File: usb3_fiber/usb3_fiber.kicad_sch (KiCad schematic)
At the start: 64 parts, among them J1 U77A16382001, J2 UE76A202000T, J3 10118194-0001LF, J4 GSB4211311WEU, J5 GSB3111311HR, Q1 MMBT3906, U1 MCP2221AT-I/ML, U2 DS100BR111SQE/NOPB, U4 LD1086D2T33TR

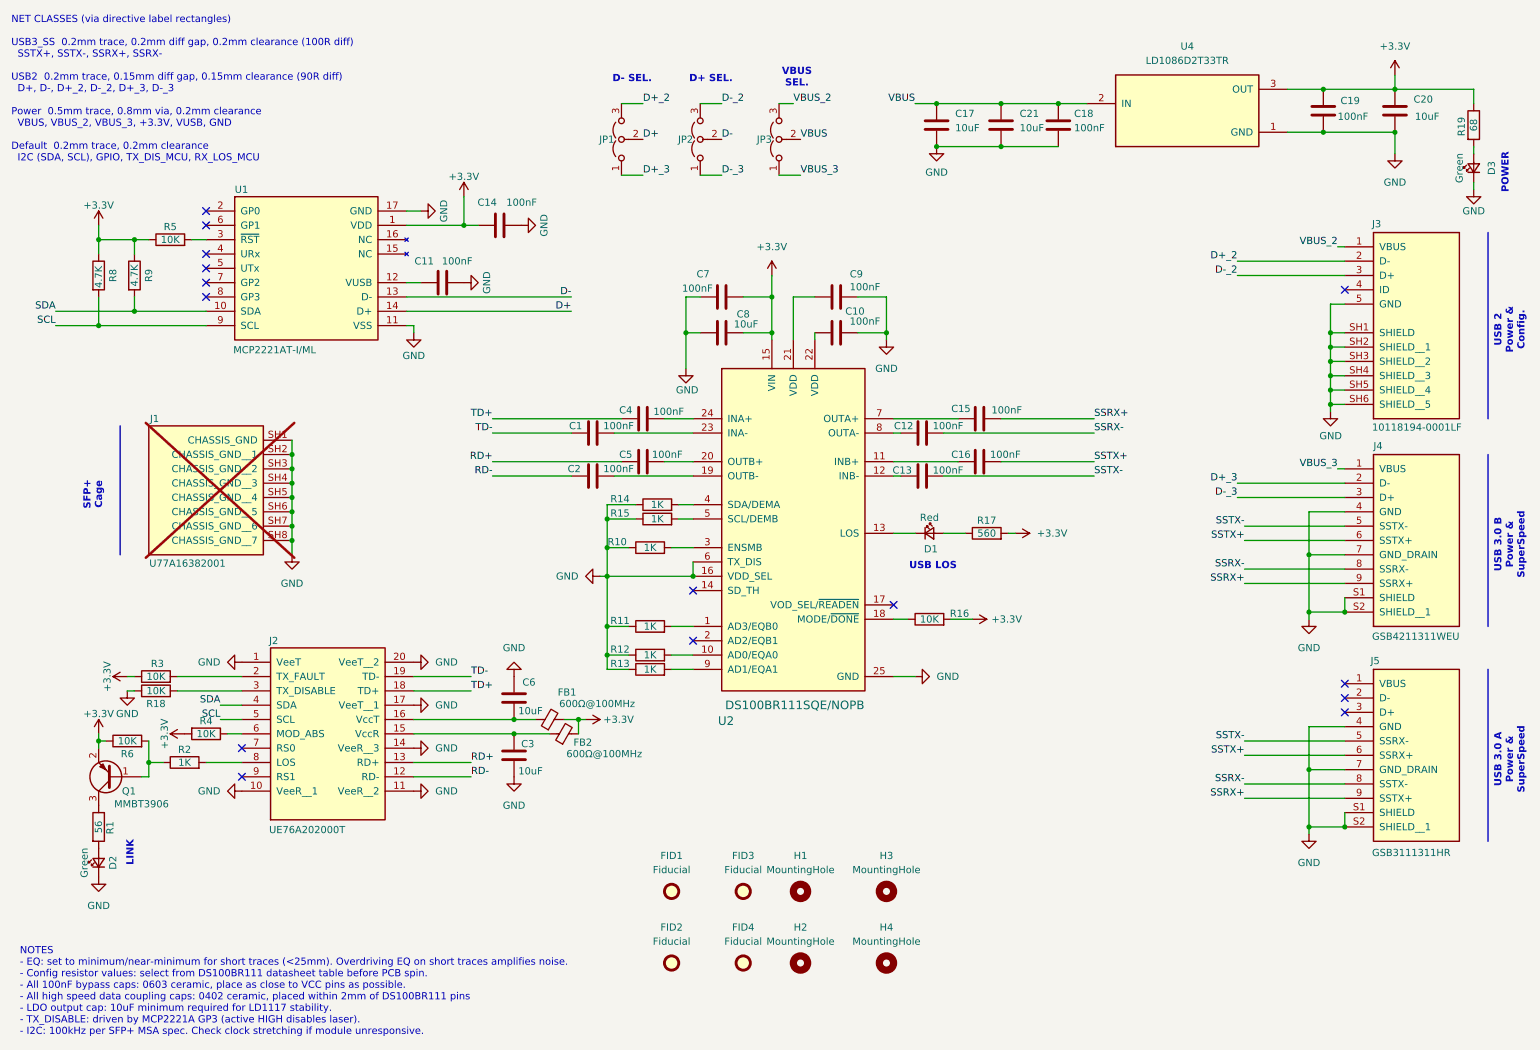
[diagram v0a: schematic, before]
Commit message: update to KiCAD 10
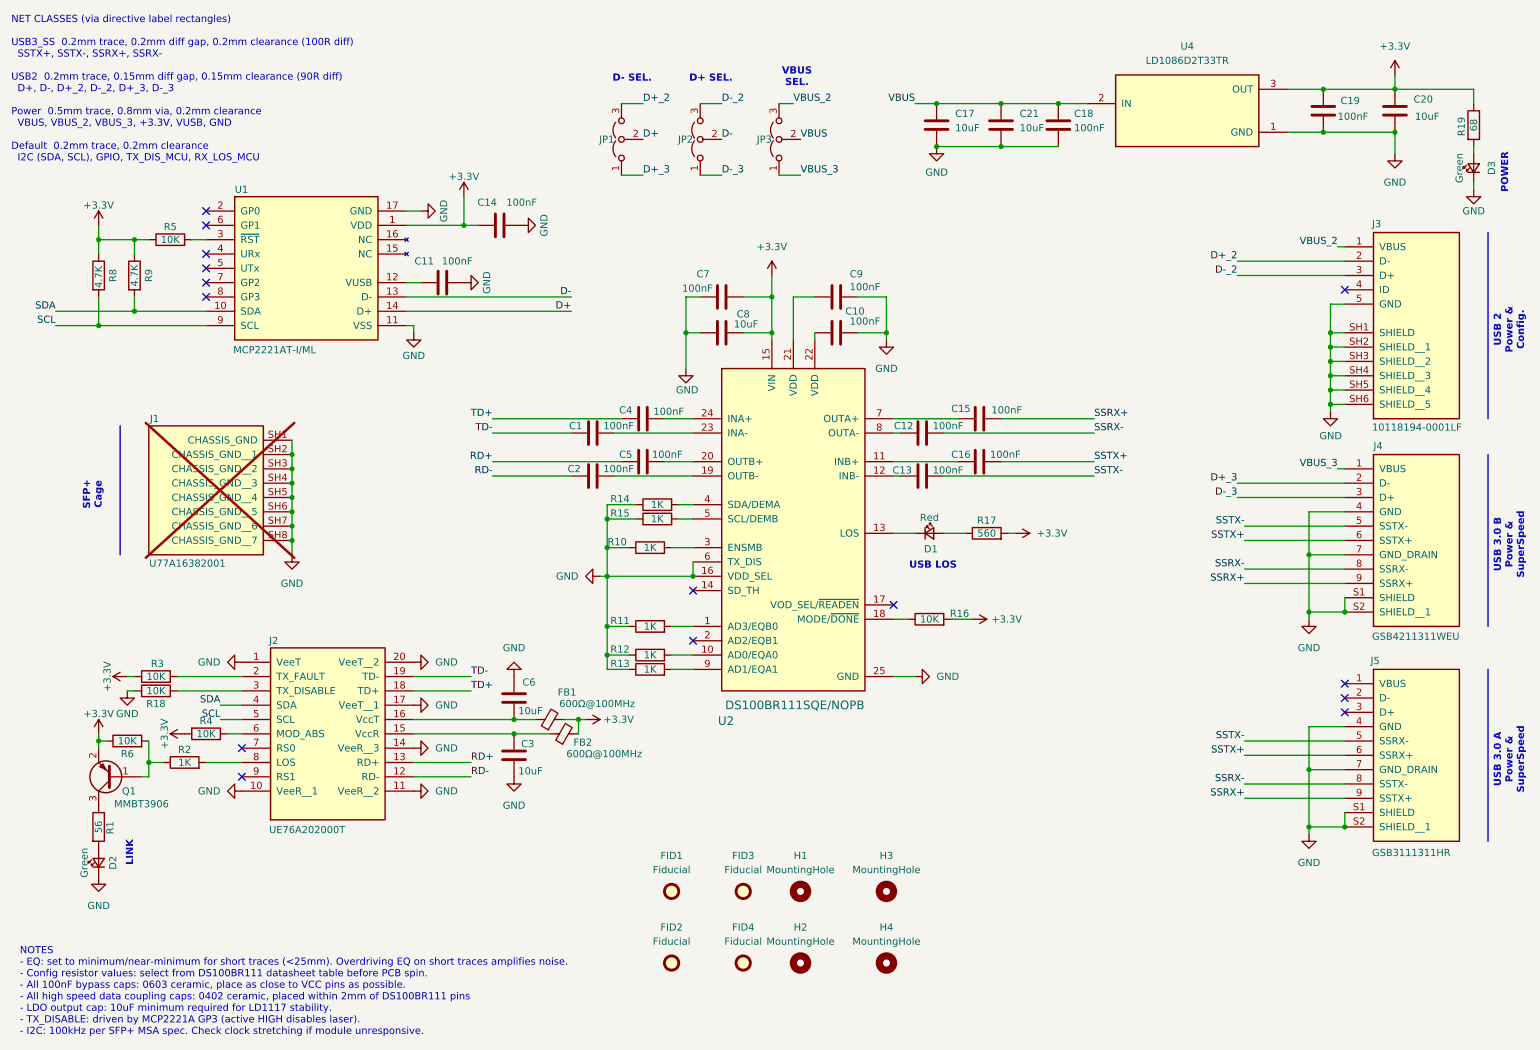
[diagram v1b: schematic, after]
